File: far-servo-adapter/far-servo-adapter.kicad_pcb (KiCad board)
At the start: 2 copper layers, 100 x 80 mm, 27 parts, among them J1 Screw_Terminal_01x02, J17 Screw_Terminal_01x02, J18 Screw_Terminal_01x02, J2 Screw_Terminal_01x02, J3 Screw_Terminal_01x02, J4 Screw_Terminal_01x02, Q1 BTA16-600BW, Q2 BTA16-600BW, Q3 BTA16-600BW, Q4 BTA16-600BW, U1 MOC3063M, U2 MOC3063M, U3 MOC3063M, U4 MOC3063M

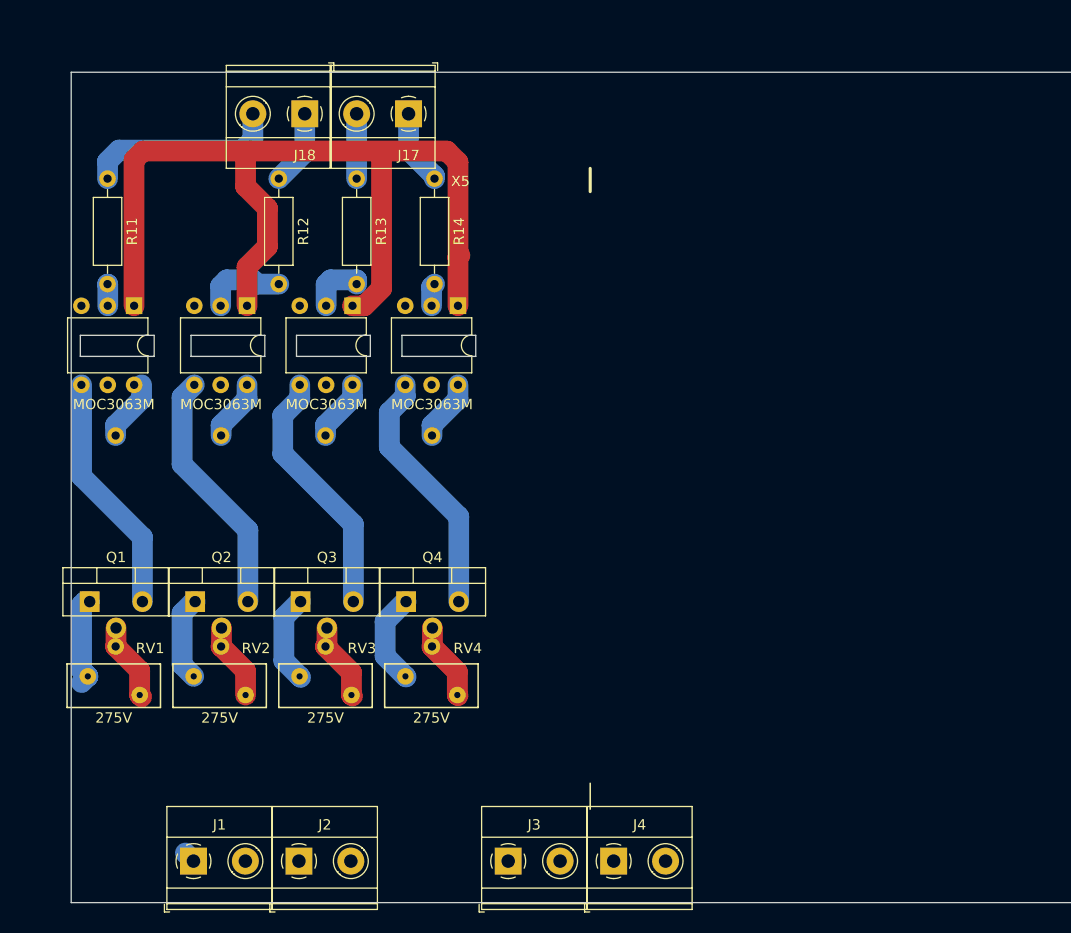
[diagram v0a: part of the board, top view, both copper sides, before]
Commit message: far-servo-adapter += terminals
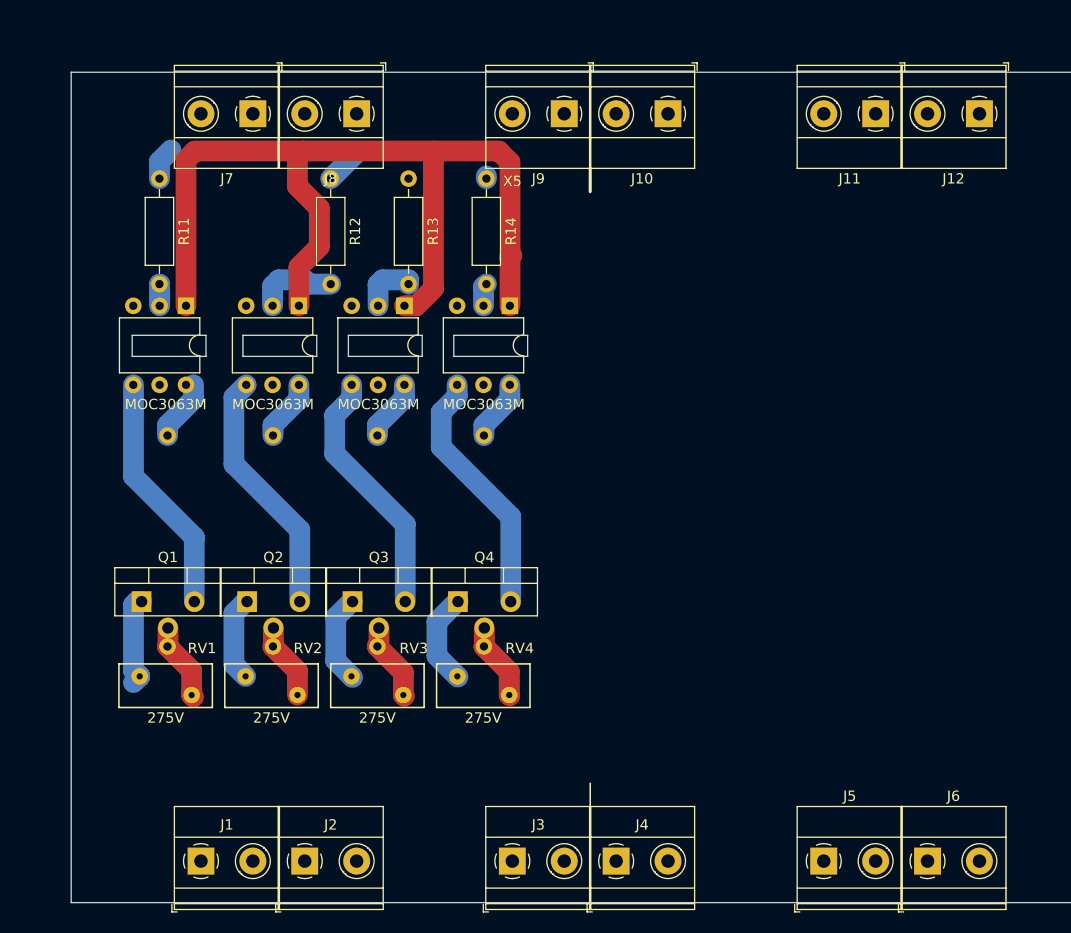
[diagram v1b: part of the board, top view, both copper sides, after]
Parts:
- removed J17, J18: Screw_Terminal_01x02, TerminalBlock_Phoenix:TerminalBlock_Phoenix_MKDS-1,5-2_1x02_P5.00mm_Horizontal
- added J10: Screw_Terminal_01x02, TerminalBlock_Phoenix:TerminalBlock_Phoenix_MKDS-1,5-2_1x02_P5.00mm_Horizontal, F.Cu at (207.5, 64.0)
- added J11: Screw_Terminal_01x02, TerminalBlock_Phoenix:TerminalBlock_Phoenix_MKDS-1,5-2_1x02_P5.00mm_Horizontal, F.Cu at (227.5, 64.0)
- added J12: Screw_Terminal_01x02, TerminalBlock_Phoenix:TerminalBlock_Phoenix_MKDS-1,5-2_1x02_P5.00mm_Horizontal, F.Cu at (237.5, 64.0)
- added J5: Screw_Terminal_01x02, TerminalBlock_Phoenix:TerminalBlock_Phoenix_MKDS-1,5-2_1x02_P5.00mm_Horizontal, F.Cu at (222.5, 136.0)
- added J6: Screw_Terminal_01x02, TerminalBlock_Phoenix:TerminalBlock_Phoenix_MKDS-1,5-2_1x02_P5.00mm_Horizontal, F.Cu at (232.5, 136.0)
- added J7: Screw_Terminal_01x02, TerminalBlock_Phoenix:TerminalBlock_Phoenix_MKDS-1,5-2_1x02_P5.00mm_Horizontal, F.Cu at (167.5, 64.0)
- added J8: Screw_Terminal_01x02, TerminalBlock_Phoenix:TerminalBlock_Phoenix_MKDS-1,5-2_1x02_P5.00mm_Horizontal, F.Cu at (177.5, 64.0)
- added J9: Screw_Terminal_01x02, TerminalBlock_Phoenix:TerminalBlock_Phoenix_MKDS-1,5-2_1x02_P5.00mm_Horizontal, F.Cu at (197.5, 64.0)
- moved Q1 5.00 mm to (156.8, 111.0)
- moved Q2 5.00 mm to (166.9, 111.0)
- moved Q3 5.00 mm to (177.1, 111.0)
- moved Q4 5.00 mm to (187.3, 111.0)
- moved R1 5.00 mm to (159.3, 95.0)
- moved R11 5.00 mm to (158.5, 70.2)
- moved R12 5.00 mm to (175.0, 70.2)
- moved R13 5.00 mm to (182.5, 70.2)
- moved R14 5.00 mm to (190.0, 70.2)
- moved R2 5.00 mm to (169.4, 95.0)
- moved R3 5.00 mm to (179.5, 95.0)
- moved R4 5.00 mm to (189.8, 95.0)
- moved RV1 5.00 mm to (161.6, 120.0)
- moved RV2 5.00 mm to (171.8, 120.0)
- moved RV3 5.00 mm to (182.0, 120.0)
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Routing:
- net /IN1: track 19.0 -> 3.21 mm
- net /IN4: track 7.29 -> 0.25 mm
- net /IN3: track 6.25 -> 0.00 mm
- net /IN2: track 7.29 -> 3.54 mm
- net unconnected-(J1-Pin_1-Pad1): track 1.10 -> 0.00 mm
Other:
- outline, holes or cut-outs redrawn

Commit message: update
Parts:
- removed H4: MountingHole, MountingHole:MountingHole_3.2mm_M3
- added C1: C_Polarized, Capacitor_THT:CP_Radial_D5.0mm_P2.50mm, F.Cu at (108.5, 83.0)
- added C2: C_Polarized, Capacitor_THT:CP_Radial_D5.0mm_P2.50mm, F.Cu at (118.5, 83.0)
- added C3: C_Polarized, Capacitor_THT:CP_Radial_D5.0mm_P2.50mm, F.Cu at (128.5, 83.0)
- added C4: C_Polarized, Capacitor_THT:CP_Radial_D5.0mm_P2.50mm, F.Cu at (139.0, 83.0)
- added R10: 100k, Resistor_THT:R_Axial_DIN0516_L15.5mm_D5.0mm_P20.32mm_Horizontal, F.Cu at (132.5, 125.2)
- added R15: 100k, Resistor_THT:R_Axial_DIN0516_L15.5mm_D5.0mm_P20.32mm_Horizontal, F.Cu at (137.5, 120.2)
- added R16: 100k, Resistor_THT:R_Axial_DIN0516_L15.5mm_D5.0mm_P20.32mm_Horizontal, F.Cu at (142.5, 125.2)
- added R5: 100k, Resistor_THT:R_Axial_DIN0516_L15.5mm_D5.0mm_P20.32mm_Horizontal, F.Cu at (107.5, 120.2)
- added R6: 100k, Resistor_THT:R_Axial_DIN0516_L15.5mm_D5.0mm_P20.32mm_Horizontal, F.Cu at (112.5, 125.2)
- added R7: 100k, Resistor_THT:R_Axial_DIN0516_L15.5mm_D5.0mm_P20.32mm_Horizontal, F.Cu at (117.5, 120.2)
- added R8: 100k, Resistor_THT:R_Axial_DIN0516_L15.5mm_D5.0mm_P20.32mm_Horizontal, F.Cu at (122.5, 125.2)
- added R9: 100k, Resistor_THT:R_Axial_DIN0516_L15.5mm_D5.0mm_P20.32mm_Horizontal, F.Cu at (127.5, 120.2)
- added TP1: TestPoint, Connector_Pin:Pin_D1.0mm_L10.0mm, F.Cu at (75.0, 79.0)
- added TP2: TestPoint, Connector_Pin:Pin_D1.0mm_L10.0mm, F.Cu at (87.0, 79.0)
- added TP4: TestPoint, Connector_Pin:Pin_D1.0mm_L10.0mm, F.Cu at (60.0, 127.0)
- added TP5: TestPoint, Connector_Pin:Pin_D1.0mm_L10.0mm, F.Cu at (70.0, 127.0)
- added TP6: TestPoint, Connector_Pin:Pin_D1.0mm_L10.0mm, F.Cu at (70.0, 124.0)
- added TP7: TestPoint, Connector_Pin:Pin_D1.0mm_L10.0mm, F.Cu at (78.0, 124.0)
- added TP8: TestPoint, Connector_Pin:Pin_D1.0mm_L10.0mm, F.Cu at (78.0, 127.0)
- added TP9: TestPoint, Connector_Pin:Pin_D1.0mm_L10.0mm, F.Cu at (92.0, 127.0)
- added U5: PC814, Package_DIP:DIP-4_W7.62mm, F.Cu at (108.7, 95.8)
- added U6: PC814, Package_DIP:DIP-4_W7.62mm, F.Cu at (118.7, 95.8)
- added U7: PC814, Package_DIP:DIP-4_W7.62mm, F.Cu at (128.7, 95.8)
- added U8: PC814, Package_DIP:DIP-4_W7.62mm, F.Cu at (138.7, 95.8)
- moved J9 110.0 mm to (87.5, 64.0)
- moved R12 105.6 mm to (69.4, 70.2)
- moved R13 102.9 mm to (79.6, 70.2)
- moved R14 100.3 mm to (89.7, 70.2)
- moved RV2 100.0 mm to (71.8, 120.0)
- moved J1 100.0 mm to (62.5, 136.0)
- moved J11 100.0 mm to (127.5, 64.0)
- moved J12 100.0 mm to (137.5, 64.0)
- moved J2 100.0 mm to (72.5, 136.0)
- moved J3 100.0 mm to (92.5, 136.0)
- moved J4 100.0 mm to (102.5, 136.0)
- moved J5 100.0 mm to (122.5, 136.0)
- moved J6 100.0 mm to (132.5, 136.0)
- moved J7 100.0 mm to (67.5, 64.0)
- moved J8 100.0 mm to (77.5, 64.0)
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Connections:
- J1 pad 1: unconnected-(J1-Pin_1-Pad1) -> /L1
- J1 pad 2: unconnected-(J1-Pin_2-Pad2) -> /L2
- J10 pad 1: unconnected-(J10-Pin_1-Pad1) -> /SENS2
- J10 pad 2: unconnected-(J10-Pin_2-Pad2) -> /SENS1
- J11 pad 1: unconnected-(J11-Pin_1-Pad1) -> /SENS3
- J11 pad 2: unconnected-(J11-Pin_2-Pad2) -> /NEG
- J12 pad 1: unconnected-(J12-Pin_1-Pad1) -> /NEG
- J12 pad 2: unconnected-(J12-Pin_2-Pad2) -> /SENS4
- J2 pad 1: unconnected-(J2-Pin_1-Pad1) -> /L3
- J2 pad 2: unconnected-(J2-Pin_2-Pad2) -> /L4
- J3 pad 1: unconnected-(J3-Pin_1-Pad1) -> /L
- J3 pad 2: unconnected-(J3-Pin_2-Pad2) -> /N
- J4 pad 1: unconnected-(J4-Pin_1-Pad1) -> /N
- J4 pad 2: unconnected-(J4-Pin_2-Pad2) -> /N
- J5 pad 1: unconnected-(J5-Pin_1-Pad1) -> /LSENS1
- J5 pad 2: unconnected-(J5-Pin_2-Pad2) -> /LSENS2
- J6 pad 1: unconnected-(J6-Pin_1-Pad1) -> /LSENS3
- J6 pad 2: unconnected-(J6-Pin_2-Pad2) -> /LSENS4
- J7 pad 1: unconnected-(J7-Pin_1-Pad1) -> /IN2
- J7 pad 2: unconnected-(J7-Pin_2-Pad2) -> /IN1
- J8 pad 1: unconnected-(J8-Pin_1-Pad1) -> /IN3
- J8 pad 2: unconnected-(J8-Pin_2-Pad2) -> /IPOS1
- J9 pad 1: unconnected-(J9-Pin_1-Pad1) -> /IPOS2
- J9 pad 2: unconnected-(J9-Pin_2-Pad2) -> /IN4
- Q1 pad 1: Net-(Q1-A1) -> /L1
- Q1 pad 2: Net-(Q1-A2) -> /L
- Q2 pad 1: Net-(Q2-A1) -> /L2
- Q2 pad 2: Net-(Q2-A2) -> /L
- Q3 pad 1: Net-(Q3-A1) -> /L3
- Q3 pad 2: Net-(Q3-A2) -> /L
- Q4 pad 1: Net-(Q4-A1) -> /L4
- Q4 pad 2: Net-(Q4-A2) -> /L
- R1 pad 2: Net-(Q1-A2) -> /L
- R2 pad 2: Net-(Q2-A2) -> /L
- R3 pad 2: Net-(Q3-A2) -> /L
- R4 pad 2: Net-(Q4-A2) -> /L
- RV1 pad 1: Net-(Q1-A2) -> /L
- RV1 pad 2: Net-(Q1-A1) -> /L1
- RV2 pad 1: Net-(Q2-A2) -> /L
- RV2 pad 2: Net-(Q2-A1) -> /L2
- RV3 pad 1: Net-(Q3-A2) -> /L
- RV3 pad 2: Net-(Q3-A1) -> /L3
- RV4 pad 1: Net-(Q4-A2) -> /L
- RV4 pad 2: Net-(Q4-A1) -> /L4
- U1 pad 1: /VHL -> /IPOS1
- U2 pad 1: /VHL -> /IPOS1
- U3 pad 1: /VHL -> /IPOS2
- U4 pad 1: /VHL -> /IPOS2
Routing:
- net /NEG: track 0.00 -> 112.3 mm, vias 0 -> 6
- net /L: track 0.00 -> 102.5 mm
- net /VHL: track 93.7 -> 0.00 mm
- net /N: track 0.00 -> 61.1 mm, vias 0 -> 1
- net /IPOS1: track 0.00 -> 37.6 mm
- net /IPOS2: track 0.00 -> 34.8 mm
- net /L1: track 0.00 -> 30.9 mm
- net /L4: track 0.00 -> 30.8 mm
- net /L3: track 0.00 -> 28.4 mm
- net /L2: track 0.00 -> 27.0 mm
- net /SENS4: track 0.00 -> 27.0 mm
- net /SENS1: track 0.00 -> 25.9 mm
- net /LSENS1: track 0.00 -> 25.9 mm
- net /SENS3: track 0.00 -> 24.7 mm
- net /SENS2: track 0.00 -> 24.7 mm
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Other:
- outline, holes or cut-outs redrawn
- board text added: "230V side"
- board text added: "24V side"
- board text added: "IPOS1"
- board text added: "IPOS2"
- board text added: "L"
- board text added: "N"
- board text added: "ONEG1"
- board text added: "ONEG2"
- board text added: "VALVE1_ENGAGE"
- board text added: "VALVE1_L"
- board text added: "VALVE1_L_IF_CLOSED"
- board text added: "VALVE1_L_IF_OPEN"
- board text added: "VALVE1_N"
- board text added: "VALVE2_ENGAGE"
- board text added: "VALVE2_L"
- board text added: "VALVE2_L_IF_CLOSED"
- board text added: "VALVE2_L_IF_OPEN"
- board text added: "VALVE2_M"
- board text removed: "X5"
